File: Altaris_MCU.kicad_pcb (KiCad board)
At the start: 4 copper layers, 101.1 x 69.8 mm, 70 parts, among them J1 Screw_Terminal_01x02, J11 Screw_Terminal_01x02, J12 Screw_Terminal_01x02, J13 Screw_Terminal_01x02, J14 Screw_Terminal_01x02, J15 Screw_Terminal_01x02, J2 Conn_01x04_Pin, J3 Screw_Terminal_01x02, J4 Screw_Terminal_01x02, J5 Conn_01x04_Pin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

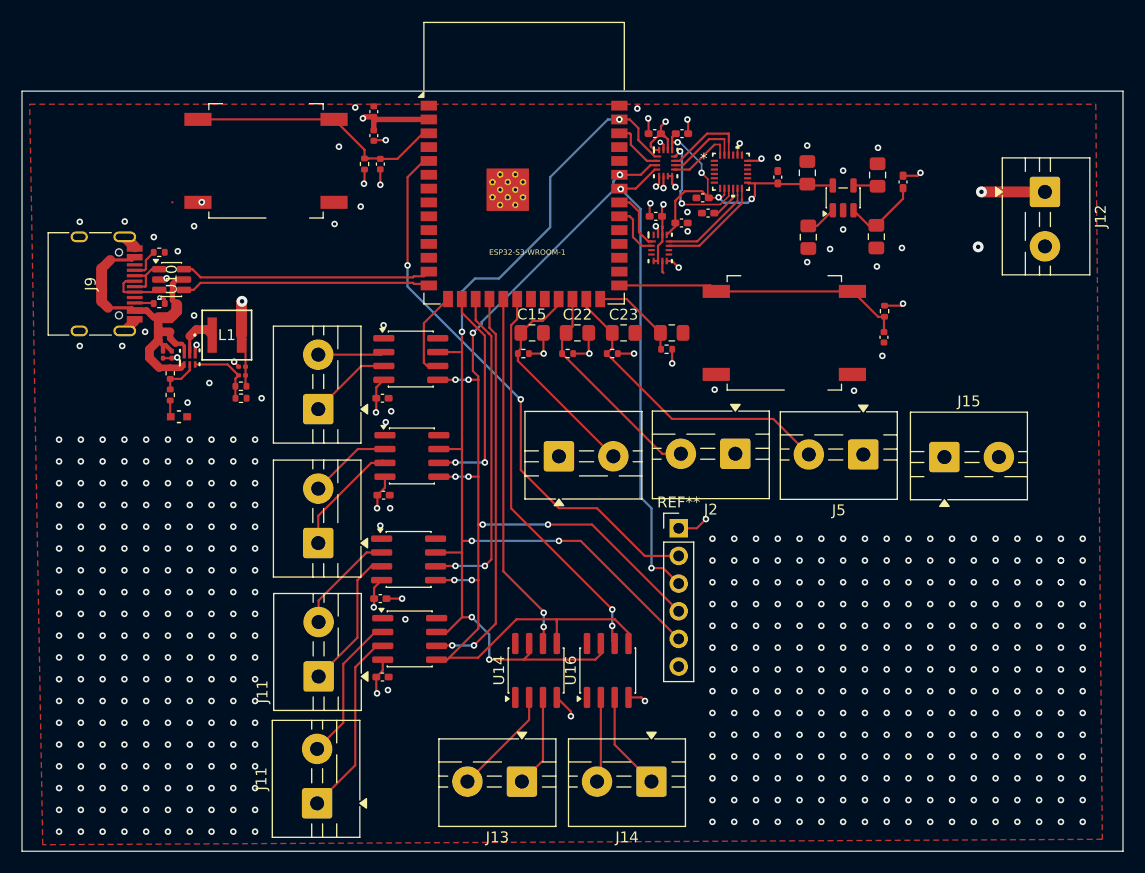
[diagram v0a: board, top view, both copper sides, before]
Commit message: Cleaned up schematic, added 5V screw terminal and 3.3V buck converter, added some test led, ran DRC and fixed connections
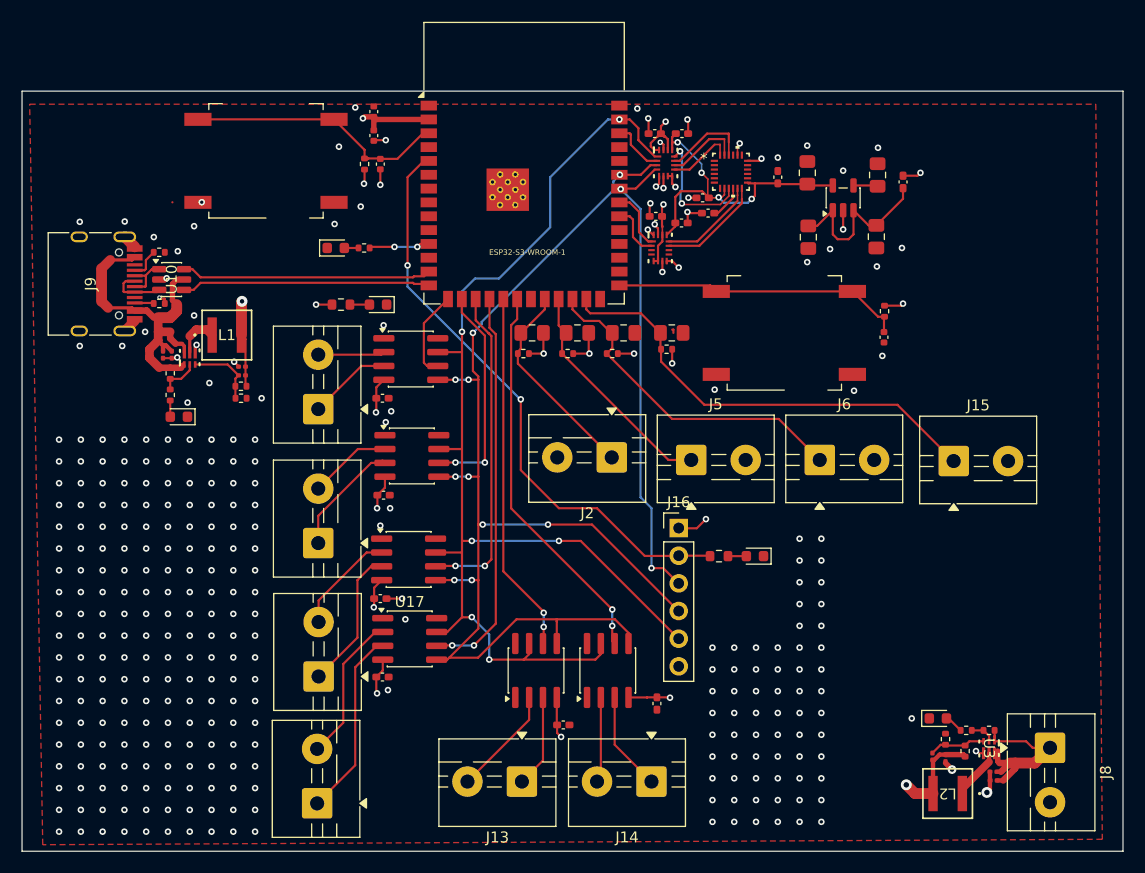
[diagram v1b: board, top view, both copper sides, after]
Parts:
- removed J12: Screw_Terminal_01x02, TerminalBlock:TerminalBlock_MaiXu_MX126-5.0-02P_1x02_P5.00mm
- removed REF**: PinHeader_1x06_P2.54mm_Vertical, Connector_PinHeader_2.54mm:PinHeader_1x06_P2.54mm_Vertical
- removed U14, U16: MAX31855KASA, Package_SO:SOIC-8_3.9x4.9mm_P1.27mm
- added C1: 0.1u, Capacitor_SMD:C_0201_0603Metric, F.Cu at (189.9, 130.2)
- added C10: 120p, Capacitor_SMD:C_0201_0603Metric, F.Cu at (184.3, 128.8)
- added C28: 0.1uF, Capacitor_SMD:C_0402_1005Metric_Pad0.74x0.62mm_HandSolder, F.Cu at (150.4, 125.9)
- added C29: 0.1uF, Capacitor_SMD:C_0402_1005Metric_Pad0.74x0.62mm_HandSolder, F.Cu at (159.0, 123.9)
- added C5: 4.7u, Capacitor_SMD:C_0201_0603Metric, F.Cu at (189.9, 131.0)
- added C7: 30u, Capacitor_SMD:C_0201_0603Metric, F.Cu at (185.5, 128.9)
- added D2: LED, LED_SMD:LED_0603_1608Metric, F.Cu at (168.0, 110.4)
- added J16: Conn_01x06, Connector_PinHeader_2.54mm:PinHeader_1x06_P2.54mm_Vertical, F.Cu at (161.0, 107.8)
- added J8: Screw_Terminal_01x02, TerminalBlock:TerminalBlock_MaiXu_MX126-5.0-02P_1x02_P5.00mm, F.Cu at (195.1, 128.0)
- added L2: 0.47u, MyFootprints:IND_XFL4015_COC, F.Cu at (185.7, 132.2)
- added LED2: LTST-C190KRKT, LED_SMD:LED_0603_1608Metric, F.Cu at (115.1, 97.6)
- added LED3: LTST-C190KRKT, LED_SMD:LED_0603_1608Metric, F.Cu at (133.4, 87.3)
- added LED4: LTST-C190KRKT, LED_SMD:LED_0603_1608Metric, F.Cu at (129.5, 82.1)
- added R12: 1k, Resistor_SMD:R_0402_1005Metric, F.Cu at (132.1, 82.1)
- added R13: 100k, Resistor_SMD:R_0402_1005Metric, F.Cu at (189.5, 126.4)
- added R14: 4.7k, Resistor_SMD:R_0402_1005Metric, F.Cu at (187.4, 126.4)
- added R16: 1k, Resistor_SMD:R_0603_1608Metric, F.Cu at (164.7, 110.4)
- added R17: 1k, Resistor_SMD:R_0603_1608Metric, F.Cu at (130.0, 87.3)
- added R18: 450k, Resistor_SMD:R_0402_1005Metric, F.Cu at (187.3, 128.3)
- added R19: 100k, Resistor_SMD:R_0402_1005Metric, F.Cu at (185.5, 127.2)
- added U17: MAX31855TASA, Package_SO:SOIC-8_3.9x4.9mm_P1.27mm, F.Cu at (136.3, 118.0)
- added U18: MAX31855TASA, Package_SO:SOIC-8_3.9x4.9mm_P1.27mm, F.Cu at (147.9, 120.9)
- added U3: TPS62827DMQT, MyFootprints:DMQ0006A, F.Cu at (189.5, 128.1)
- J2, J5, J6: value Conn_01x04_Pin -> Screw_Terminal_01x02
- LED1: footprint MyFootprints:LED_LTST-C190_LTO -> LED_SMD:LED_0603_1608Metric
- R11: value 1k -> 4.7k
- U11: value MAX31855KASA -> MAX31855TASA
- moved LED1 75.0 mm to (184.8, 125.3), turned to 0 degrees
- moved J6 24.0 mm to (173.9, 101.6)
- moved U11 18.4 mm to (154.5, 120.9), turned to 90 degrees
- moved J5 15.8 mm to (162.2, 101.6), turned to 0 degrees
- moved J2 11.4 mm to (154.8, 101.3)
- moved J15 0.93 mm to (186.2, 101.7)
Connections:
- J2 pad 1: Common2 -> ADC_IN1
- J2 pad 2: ADC_IN2 -> Common1
- J5 pad 1: Common3 -> ADC_IN2
- J5 pad 2: ADC_IN3 -> Common2
- J6 pad 1: Common1 -> ADC_IN3
- J6 pad 2: ADC_IN1 -> Common3
- LED1 pad 2: Net-(LED1-Pad2) -> Net-(LED1-A)
- R11 pad 1: Net-(LED1-Pad2) -> Net-(LED2-A)
- U1 pad 11: unconnected-(U1-IO18-Pad11) -> TESTLED
- U1 pad 22: TESTLED -> ADC_IN1
- U1 pad 23: ADC_IN1 -> ADC_IN2
- U1 pad 24: ADC_IN2 -> ADC_IN3
- U1 pad 25: ADC_IN3 -> ADC_IN4
- U1 pad 26: ADC_IN4 -> unconnected-(U1-IO45-Pad26)
- U11 pad 2: T4- -> T6-
- U11 pad 3: T4+ -> T6+
- U11 pad 6: MAX_CS4 -> MAX_CS6
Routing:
- net ADC_IN4: track 8.80 -> 42.0 mm
- net +5V_b: track 0.00 -> 17.0 mm
- net +3.3V_b: track 59.7 -> 69.7 mm, vias 17 -> 19
- net GND: track 34.2 -> 42.9 mm, vias 505 -> 319
- net Net-(U5-EN): track 10.4 -> 17.1 mm
- net TESTLED: track 0.00 -> 5.58 mm, vias 0 -> 2
- net Net-(U3-FB): track 0.00 -> 5.21 mm
- net Net-(U3-SW): track 0.00 -> 4.72 mm
- net SD_CS: track 51.7 -> 54.6 mm
- net ADC_IN3: track 28.7 -> 31.3 mm
- net Net-(U3-PG): track 0.00 -> 2.29 mm
- net Net-(LED3-A): track 0.00 -> 1.79 mm
- net Net-(D2-A): track 0.00 -> 1.69 mm
- net Net-(LED1-A): track 0.00 -> 1.56 mm
- net Net-(LED1-Pad2): track 1.51 -> 0.00 mm
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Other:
- board text removed: "J11"

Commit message: finalized pcb
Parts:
- moved R17 11.4 mm to (135.7, 97.2)
- moved LED3 11.3 mm to (138.8, 97.2)
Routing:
- net GND: track 42.9 -> 45.5 mm
- net +3.3V_b: track 69.7 -> 69.9 mm, vias 19 -> 18
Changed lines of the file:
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@@
 			(at 2.25 -5.12 90)
 			(layer "F.SilkS")
+			(hide yes)
 			(effects
 				(font
@@
 	(footprint "LED_SMD:LED_0603_1608Metric"
 		(layer "F.Cu")
-		(at 133.3875 87.3 180)
+		(at 138.8 97.2 180)
 		(descr "LED SMD 0603 (1608 Metric), square (rectangular) end terminal, IPC-7351 nominal, (Body size source: http://www.tortai-tech.com/upload/download/2011102023233369053.pdf), generated with kicad-footprint-generator")
 		(tags "LED")
@@
 	(footprint "Resistor_SMD:R_0603_1608Metric"
 		(layer "F.Cu")
-		(at 129.9875 87.3)
+		(at 135.675 97.2)
 		(descr "Resistor SMD 0603 (1608 Metric), square (rectangular) end terminal, IPC-7351 nominal, (Body size source: IPC-SM-782 page 72, https://www.pcb-3d.com/wordpress/wp-content/uploads/ipc-sm-782a_amendment_1_and_2.pdf), generated with kicad-footprint-generator")
 		(tags "resistor")
@@
 	)
 	(segment
+		(start 139.5875 95.9125)
+		(end 139.6 95.9)
+		(width 0.2)
+		(layer "F.Cu")
+		(net 1)
+	)
+	(segment
 		(start 111.045 88.65)
 		(end 111.045 88.805)
@@
 	)
 	(segment
+		(start 135.5 95.9)
+		(end 135.6 95.8)
+		(width 0.2)
+		(layer "F.Cu")
+		(net 1)
+	)
+	(segment
 		(start 160.4 83.3)
 		(end 161 83.9)
@@
 	)
 	(segment
+		(start 134.365 95.9)
+		(end 135.5 95.9)
+		(width 0.2)
+		(layer "F.Cu")
+		(net 1)
+	)
+	(segment
 		(start 161.825001 79.805)
 		(end 161.825001 78.825001)
@@
 	)
 	(segment
+		(start 139.5875 97.2)
+		(end 139.5875 95.9125)
+		(width 0.2)
+		(layer "F.Cu")
+		(net 1)
+	)
+	(segment
 		(start 166.399999 72.700001)
 		(end 166.6 72.5)
@@
 	)
 	(via
+		(at 139.6 95.9)
+		(size 0.6)
+		(drill 0.3)
+		(layers "F.Cu" "B.Cu")
+		(net 1)
+	)
+	(via
 		(at 172.1 134.8)
 		(size 0.6)
@@
 	)
 	(via
-		(at 122.1 113.7)
+		(at 135.6 95.8)
 		(size 0.6)
 		(drill 0.3)
@@
 	)
 	(via
-		(at 106.1 117.7)
+		(at 122.1 113.7)
 		(size 0.6)
 		(drill 0.3)
@@
 	)
 	(via
-		(at 106.1 121.7)
+		(at 106.1 117.7)
 		(size 0.6)
 		(drill 0.3)
@@
 	)
 	(via
-		(at 168.1 132.8)
+		(at 106.1 121.7)
 		(size 0.6)
 		(drill 0.3)
@@
 	)
 	(via
-		(at 168.6 73.9)
+		(at 168.1 132.8)
 		(size 0.6)
 		(drill 0.3)
@@
 	)
 	(via
-		(at 134.6 97.1)
+		(at 168.6 73.9)
 		(size 0.6)
 		(drill 0.3)
@@
 	)
 	(via
-		(at 134.1 98.1)
-		(size 0.6)
-		(drill 0.3)
-		(layers "F.Cu" "B.Cu")
-		(net 1)
-	)
-	(via
 		(at 116.1 121.7)
 		(size 0.6)
@@
 	)
 	(via
-		(at 133.9 89.2)
+		(at 134 89.1)
 		(size 0.6)
 		(drill 0.3)
@@
 	)
 	(segment
-		(start 129.1625 87.3)
-		(end 127.7 87.3)
-		(width 0.2)
-		(layer "F.Cu")
-		(net 2)
-	)
-	(segment
 		(start 158.645962 80.9)
 		(end 158.16176 80.415798)
@@
 	)
 	(segment
+		(start 133.2 97.2)
+		(end 134.85 97.2)
+		(width 0.2)
+		(layer "F.Cu")
+		(net 2)
+	)
+	(segment
 		(start 158.99 123.375)
 		(end 159 123.365)
@@
 	)
 	(via
-		(at 127.7 87.3)
-		(size 0.6)
-		(drill 0.3)
-		(layers "F.Cu" "B.Cu")
-		(net 2)
-	)
-	(via
 		(at 181.9 131.4)
 		(size 1)
@@
 	)
 	(segment
-		(start 130.8125 87.3)
-		(end 132.6 87.3)
+		(start 136.5 97.2)
+		(end 138.0125 97.2)
 		(width 0.2)
 		(layer "F.Cu")

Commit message: final pcb
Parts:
- added LED5: LTST-C190KRKT, LED_SMD:LED_0603_1608Metric, F.Cu at (189.0, 78.1)
- added R20: 1k, Resistor_SMD:R_0402_1005Metric, F.Cu at (186.1, 78.0)
- D2: value LED -> LTST-C190KRKT
- moved C16 2.92 mm to (161.7, 71.3)
- moved C17 2.92 mm to (164.2, 71.3)
- moved C12 2.11 mm to (165.3, 77.7)
- moved C13 2.11 mm to (165.8, 79.1)
- moved C25 2.11 mm to (163.4, 80.0)
- moved C6 2.11 mm to (181.4, 75.6)
- moved C11 2.11 mm to (172.2, 75.8)
- moved C24 2.11 mm to (161.0, 79.4)
- moved C4 2.11 mm to (175.0, 81.3)
- moved C8 2.11 mm to (174.9, 75.4)
- moved C9 2.11 mm to (181.2, 81.3)
- moved FB2 2.11 mm to (183.7, 76.2)
- moved U4 2.11 mm to (167.9, 75.3)
- moved U5 2.11 mm to (178.2, 77.7)
- moved U6 2.11 mm to (161.9, 74.5)
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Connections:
- U1 pad 12: unconnected-(U1-IO8-Pad12) -> SD_CS
- U1 pad 5: SD_CS -> unconnected-(U1-IO5-Pad5)
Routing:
- net CLK: track 111.2 -> 122.6 mm
- net MISO: track 110.8 -> 121.4 mm
- net SD_CS: track 54.6 -> 46.0 mm
- net ICM_CS: track 5.05 -> 7.24 mm
- net Net-(U5-EN): track 17.1 -> 19.0 mm
- net MOSI: track 43.0 -> 44.8 mm
- net Net-(LED5-A): track 0.00 -> 1.64 mm
- net GND: track 45.5 -> 47.1 mm, vias 319 -> 495
- net USB-: track 23.3 -> 21.7 mm
- net USB+: track 22.9 -> 21.7 mm
- net Net-(J9-D+-PadA6): track 5.25 -> 6.51 mm
- net ICM_INT: track 5.02 -> 6.26 mm
- net Net-(J9-D--PadA7): track 4.52 -> 5.75 mm
- net ICM_FSYNC: track 5.58 -> 6.76 mm
- net Net-(U10-VBUS): track 32.0 -> 32.9 mm
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
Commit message: pcb final 1
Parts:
- added LED6: LTST-C190KRKT, LED_SMD:LED_0603_1608Metric, F.Cu at (166.0, 123.4)
- added R21: 1k, Resistor_SMD:R_0603_1608Metric, F.Cu at (162.7, 123.4)
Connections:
- U1 pad 36: RXD0 -> unconnected-(U1-RXD0-Pad36)
- U1 pad 37: TXD0 -> unconnected-(U1-TXD0-Pad37)
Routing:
- net Net-(LED6-A): track 0.00 -> 1.69 mm
- net +3.3V_b: track 70.3 -> 72.0 mm
- net GND: vias 495 -> 471

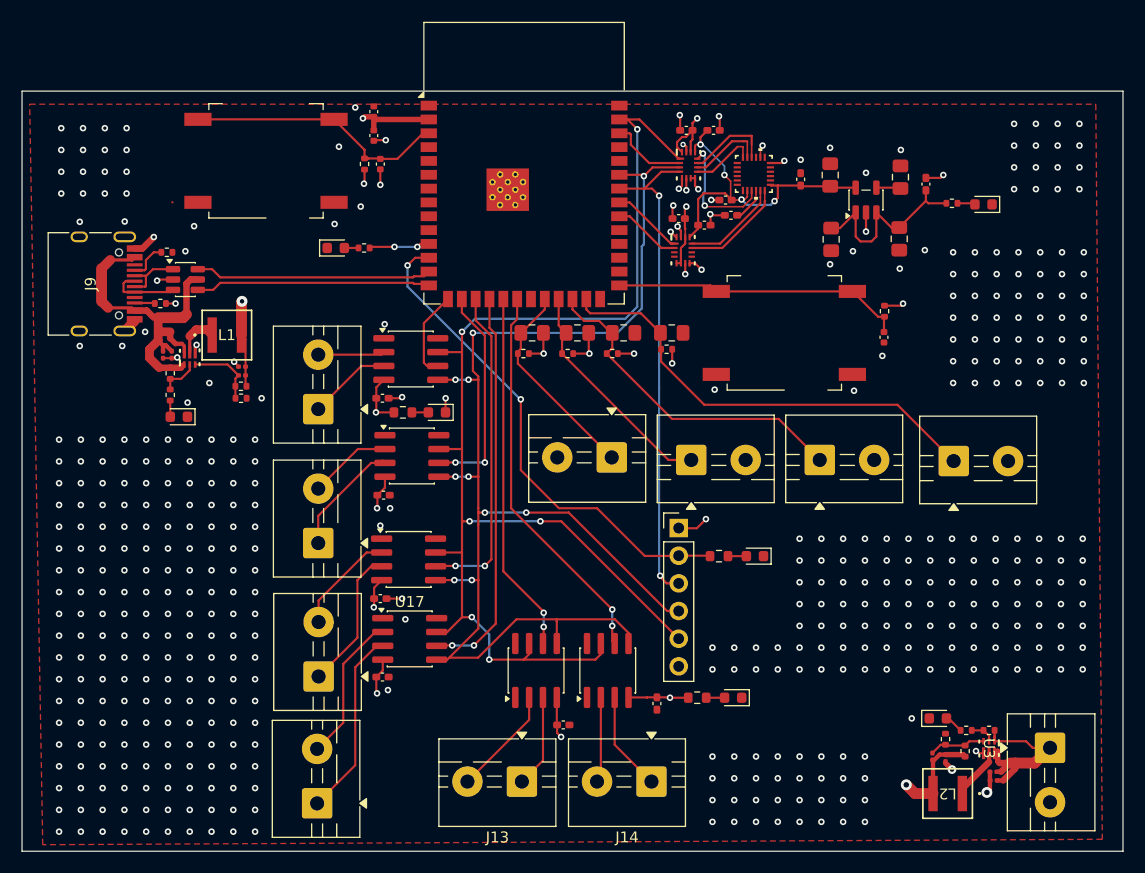
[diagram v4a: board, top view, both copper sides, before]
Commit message: edited capcitors
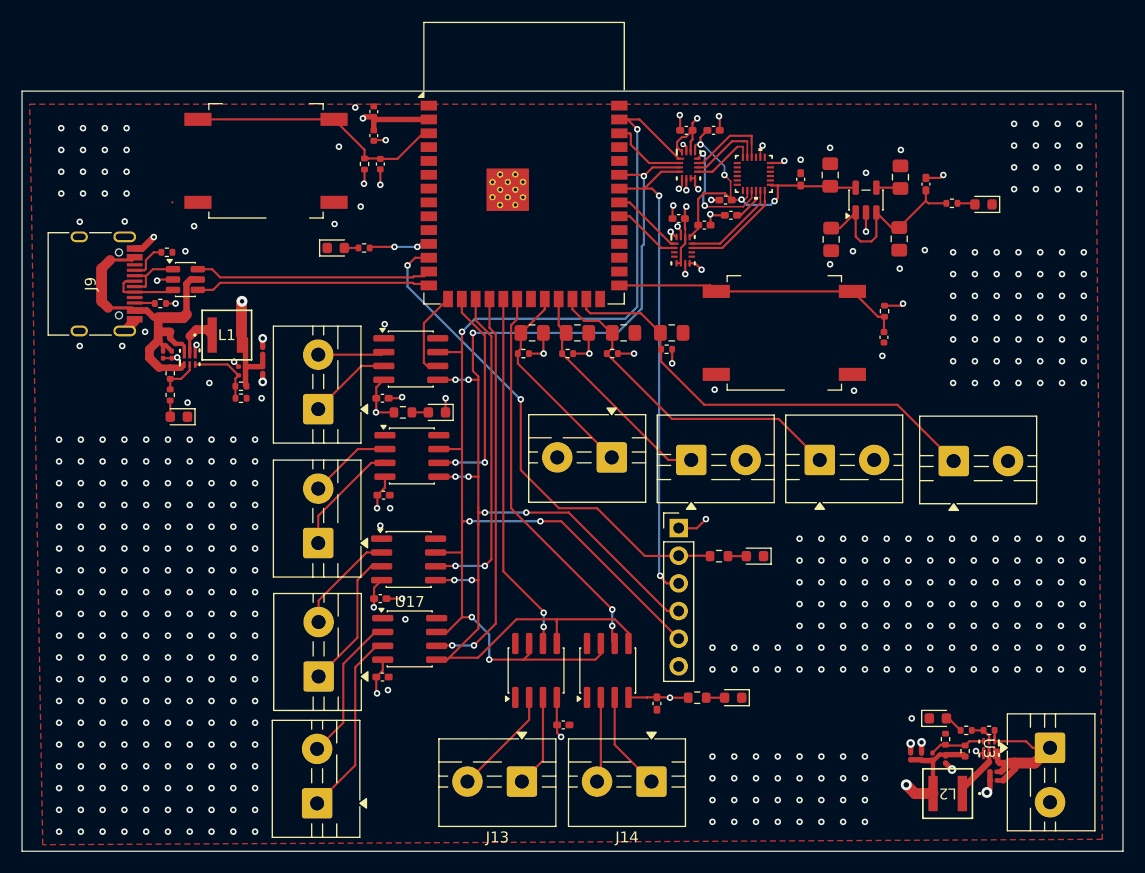
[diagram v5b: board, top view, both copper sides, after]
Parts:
- added C34: 10u, Capacitor_SMD:C_0201_0603Metric, F.Cu at (122.8, 91.5)
- added C35: 10u, Capacitor_SMD:C_0201_0603Metric, F.Cu at (122.8, 93.3)
- added C36: 10u, Capacitor_SMD:C_0201_0603Metric, F.Cu at (182.3, 128.8)
- added C37: 10u, Capacitor_SMD:C_0201_0603Metric, F.Cu at (183.3, 128.8)
- C32, C7: value 30u -> 10u
- moved C7 0.14 mm to (185.5, 129.1)
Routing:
- net +3.3V_b: track 72.0 -> 76.8 mm
- net GND: track 47.1 -> 50.5 mm, vias 471 -> 475
